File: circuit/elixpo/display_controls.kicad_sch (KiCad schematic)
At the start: 23 parts, among them J3 ST7789 320x240 module, SW11 UP, SW12 DOWN, SW13 LEFT, SW14 RIGHT, SW15 A, SW16 B, SW17 C, SW18 HOME, U6 TPS61023 5V boost

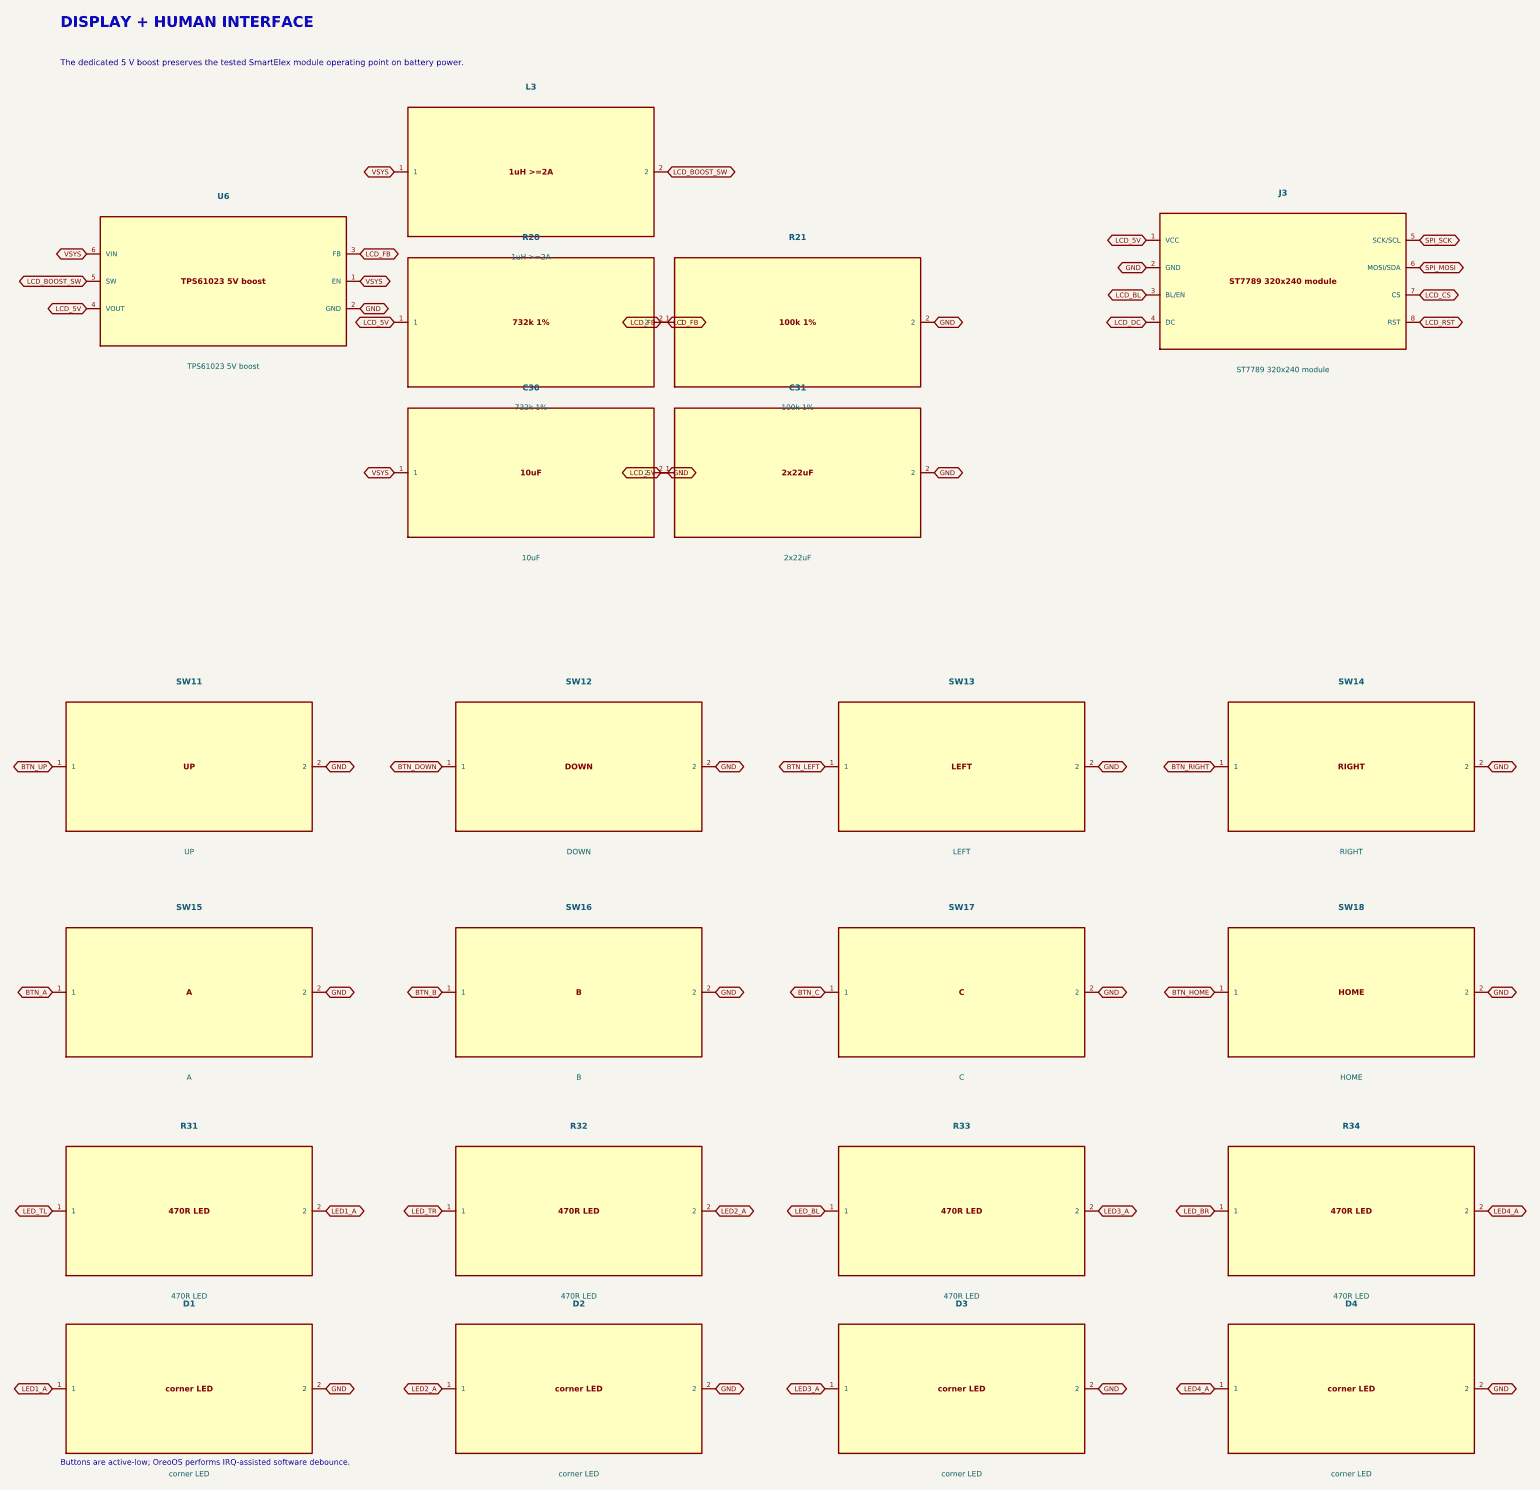
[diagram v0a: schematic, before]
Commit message: feat(hardware): complete badge schematic and procurement BOM
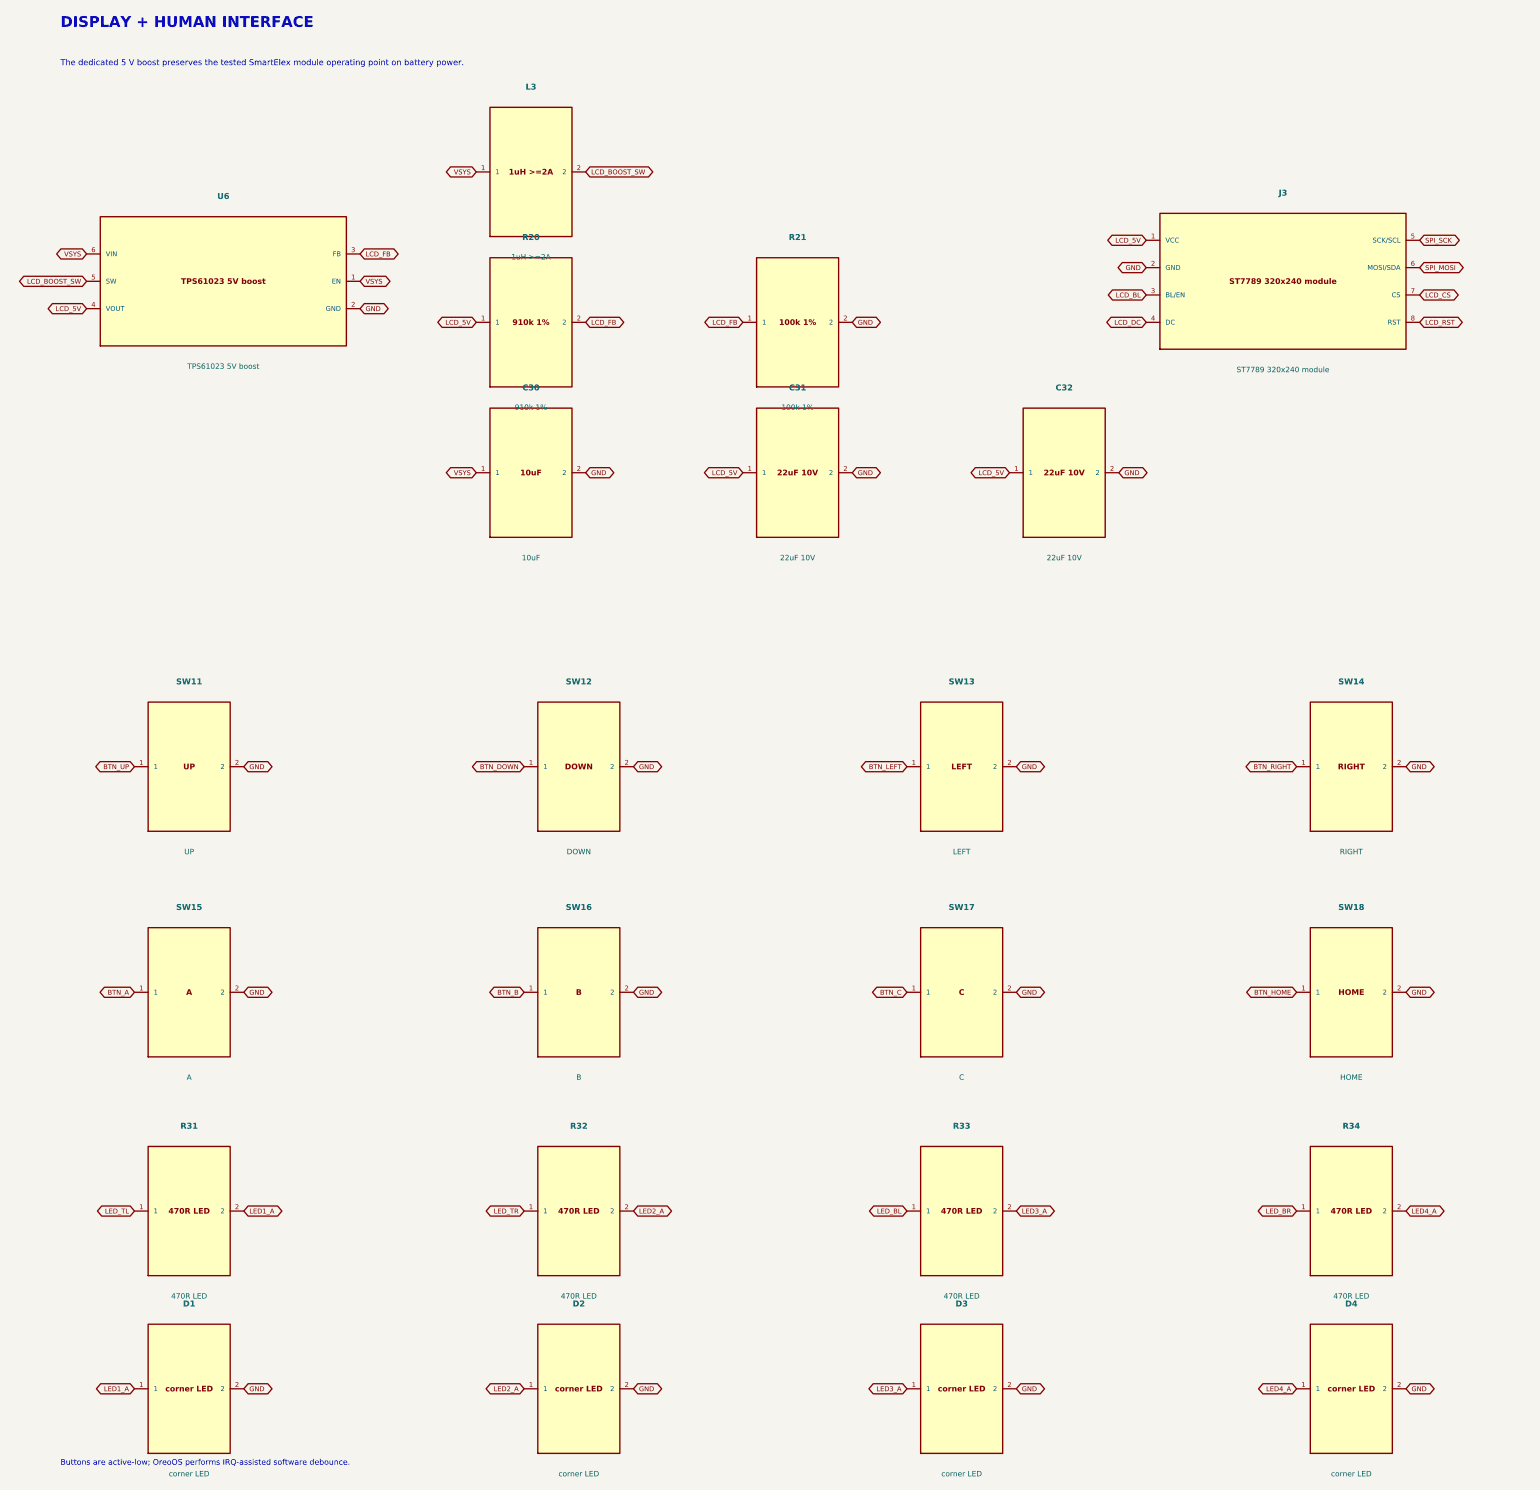
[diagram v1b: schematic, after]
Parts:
- added C32: 22uF 10V, Capacitor_SMD:C_0805_2012Metric, symbol oreo_badge:C32
- C31: value 2x22uF -> 22uF 10V
- R20: value 732k 1% -> 910k 1%
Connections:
- net GND: now also C32.2
- net LCD_5V: now also C32.1
